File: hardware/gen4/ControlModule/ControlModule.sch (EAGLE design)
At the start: 39 parts, among them IC1 XMEGA16A4A

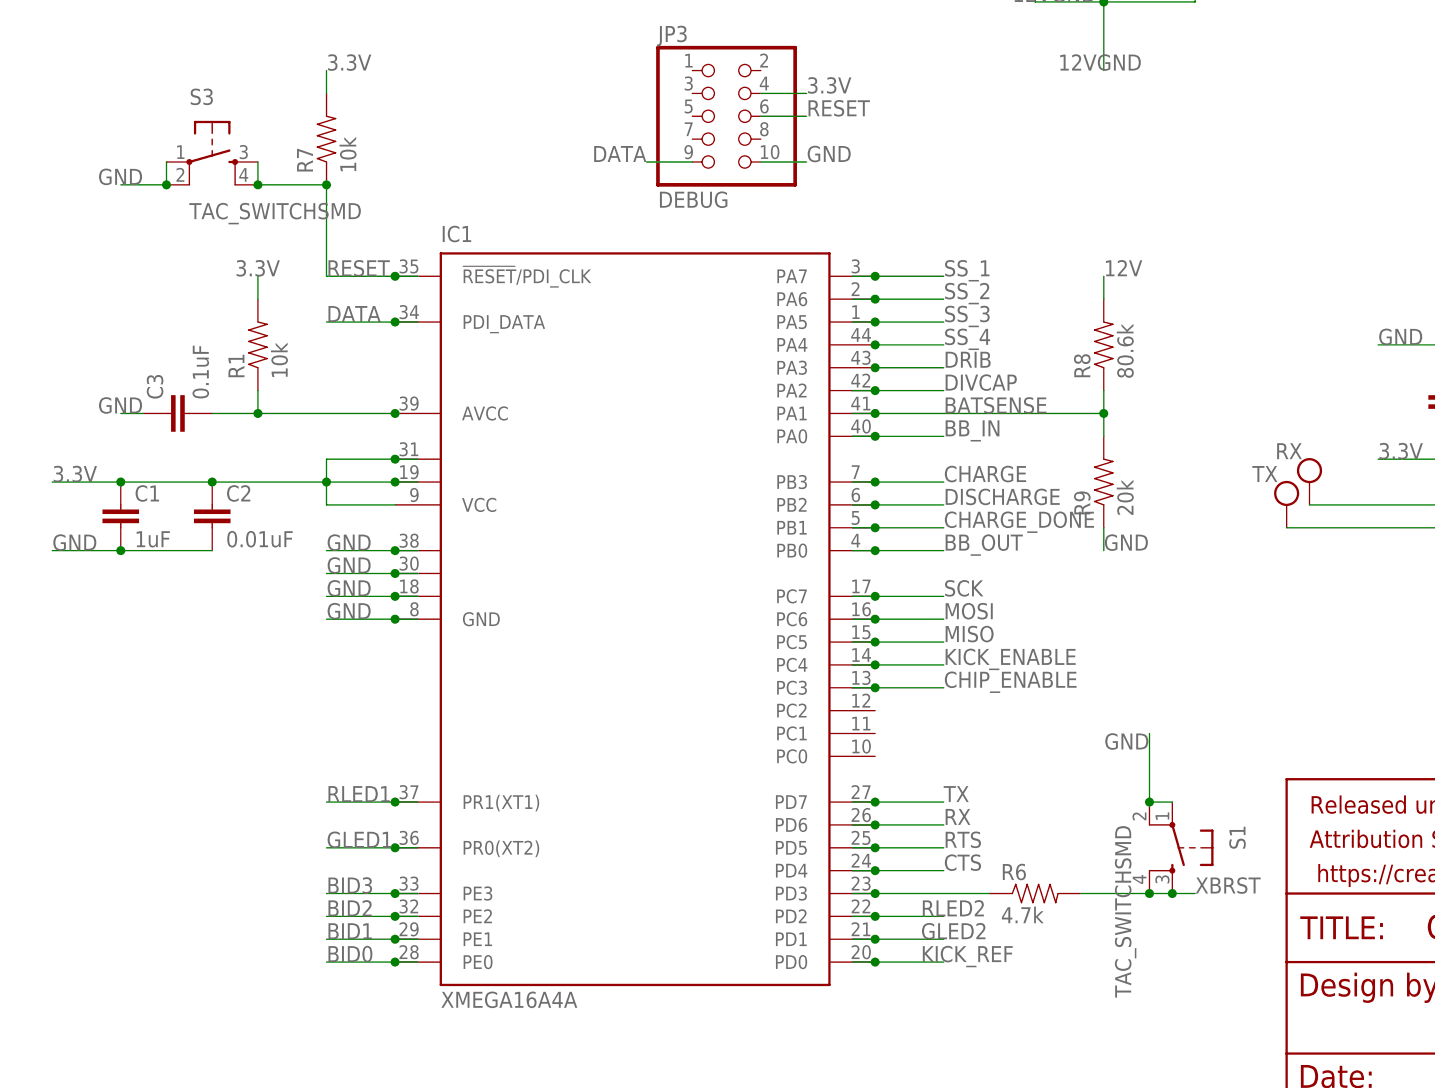
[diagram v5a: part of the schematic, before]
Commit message: fixed pushbutton on comms board
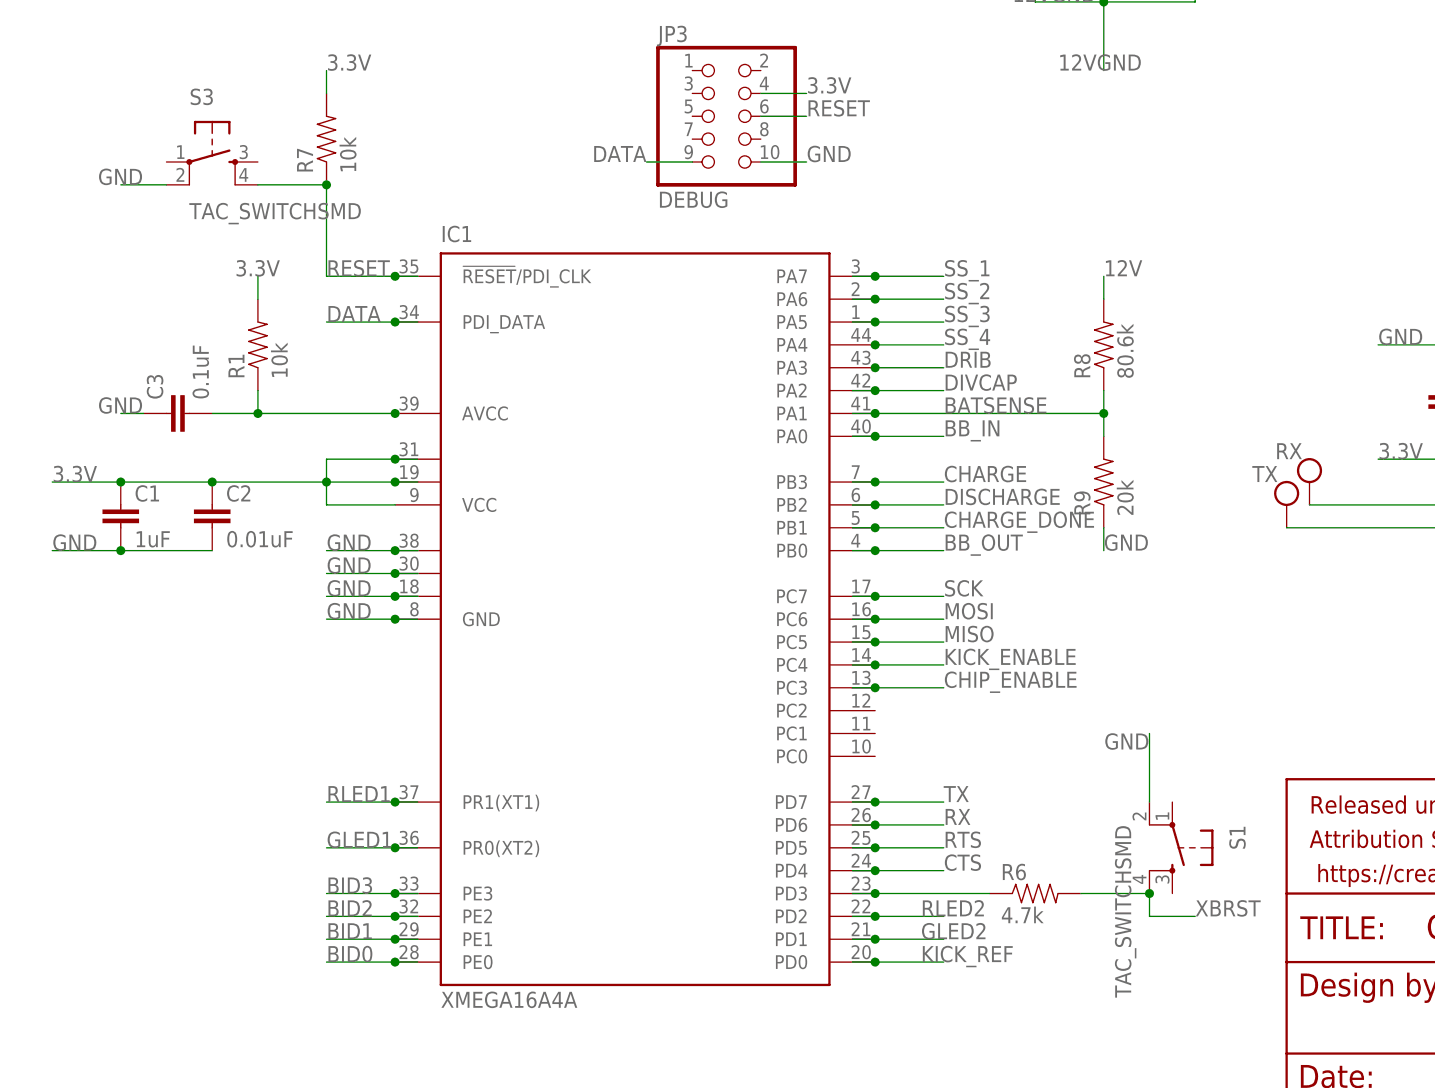
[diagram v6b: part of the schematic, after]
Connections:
- net GND: no longer S1.1, S3.1
- net RESET: no longer S3.3
- net XBRST: no longer S1.3
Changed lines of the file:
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@@
 <?xml version="1.0" encoding="utf-8"?>
 <!DOCTYPE eagle SYSTEM "eagle.dtd">
-<eagle version="7.5.0">
+<eagle version="7.2.0">
 <drawing>
 <settings>
@@
 <pinref part="R7" gate="G$1" pin="1"/>
 <pinref part="S3" gate="S" pin="4"/>
-<pinref part="S3" gate="S" pin="3"/>
-<wire x1="33.02" y1="104.14" x2="33.02" y2="101.6" width="0.1524" layer="91"/>
-<junction x="33.02" y="101.6"/>
 </segment>
 <segment>
@@
 <label x="132.08" y="40.64" size="1.778" layer="95" rot="R180"/>
 <pinref part="S1" gate="S" pin="2"/>
-<pinref part="S1" gate="S" pin="1"/>
-<wire x1="132.08" y1="33.02" x2="134.62" y2="33.02" width="0.1524" layer="91"/>
-<junction x="132.08" y="33.02"/>
 </segment>
 <segment>
@@
 <label x="15.24" y="101.6" size="1.778" layer="95"/>
 <pinref part="S3" gate="S" pin="2"/>
-<pinref part="S3" gate="S" pin="1"/>
-<wire x1="22.86" y1="104.14" x2="22.86" y2="101.6" width="0.1524" layer="91"/>
-<junction x="22.86" y="101.6"/>
 </segment>
 <segment>
@@
 <pinref part="R6" gate="G$1" pin="2"/>
 <wire x1="124.46" y1="22.86" x2="132.08" y2="22.86" width="0.1524" layer="91"/>
-<wire x1="132.08" y1="22.86" x2="134.62" y2="22.86" width="0.1524" layer="91"/>
-<label x="137.16" y="22.86" size="1.778" layer="95"/>
-<pinref part="S1" gate="S" pin="3"/>
-<wire x1="134.62" y1="22.86" x2="137.16" y2="22.86" width="0.1524" layer="91"/>
-<junction x="134.62" y="22.86"/>
+<label x="137.16" y="20.32" size="1.778" layer="95"/>
 <pinref part="S1" gate="S" pin="4"/>
 <junction x="132.08" y="22.86"/>
-</segment>
-</net>
+<wire x1="137.16" y1="20.32" x2="132.08" y2="20.32" width="0.1524" layer="91"/>
+<wire x1="132.08" y1="20.32" x2="132.08" y2="22.86" width="0.1524" layer="91"/>
+</segment>
+</net>

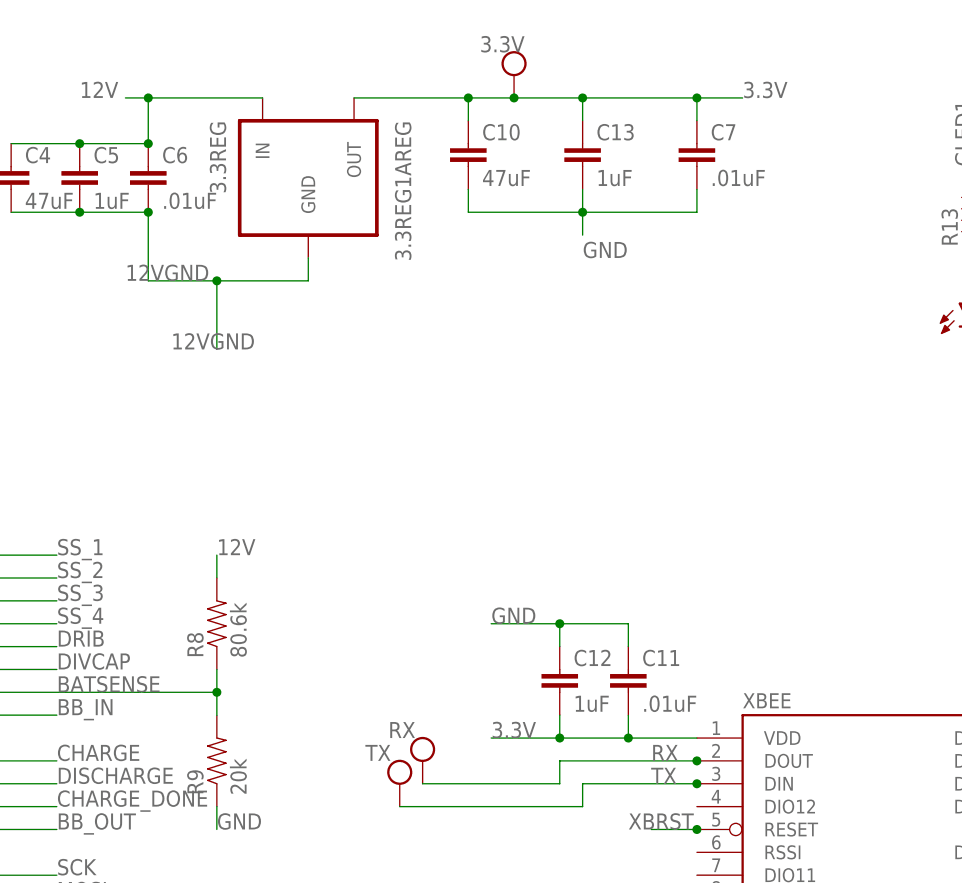
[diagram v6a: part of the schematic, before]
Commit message: fixed minor detail about capacitor sizes (using 0.01uF everywhere instead of .01uF on comms)
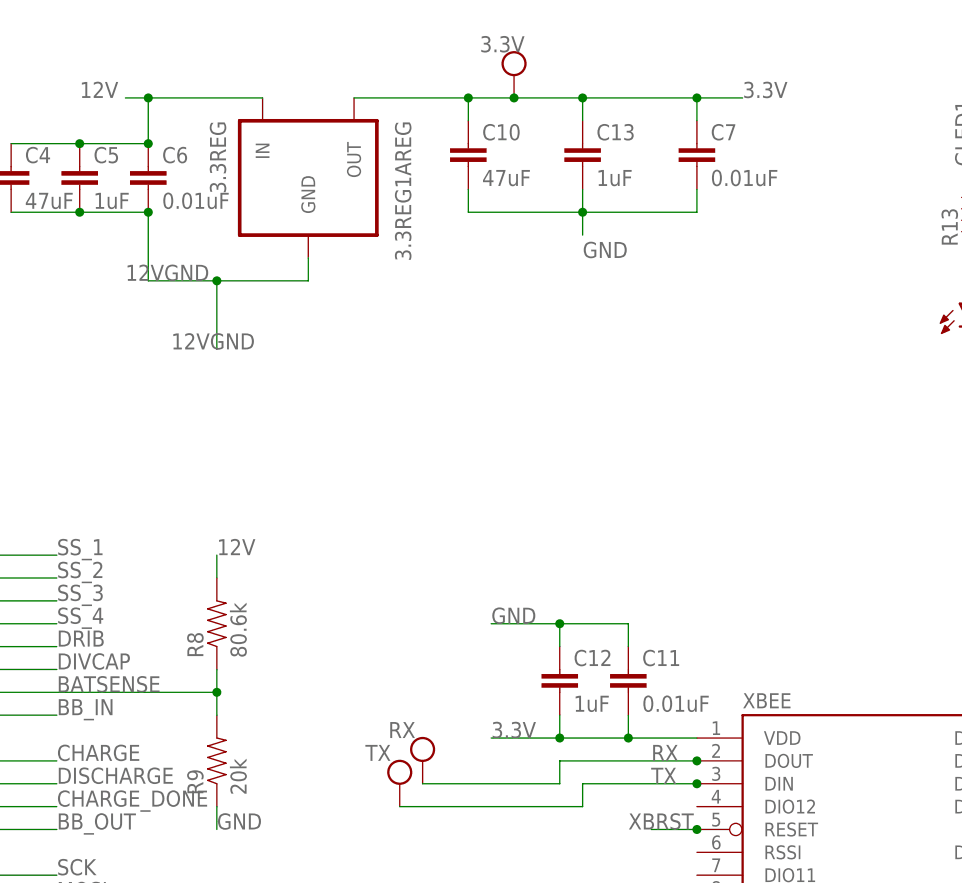
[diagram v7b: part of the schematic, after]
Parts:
- C11, C6, C7: value .01uF -> 0.01uF
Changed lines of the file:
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@@
 <part name="U$1" library="SparkFun-Electromechanical" deviceset="4-POS-DIP" device=""/>
 <part name="XBEE" library="SparkFun-RF" deviceset="XBEE-1" device="B1"/>
-<part name="C11" library="SparkFun-Capacitors" deviceset="CAP" device="0805" value=".01uF"/>
+<part name="C11" library="SparkFun-Capacitors" deviceset="CAP" device="0805" value="0.01uF"/>
 <part name="C12" library="SparkFun-Capacitors" deviceset="CAP" device="0805" value="1uF"/>
 <part name="RX" library="gen3" deviceset="TEST_PT" device=""/>
@@
 <part name="3.3V" library="gen3" deviceset="TEST_PT" device=""/>
 <part name="3.3REG" library="gen3" deviceset="3.3REG1A" device="REG"/>
-<part name="C7" library="SparkFun-Capacitors" deviceset="CAP" device="0805" value=".01uF"/>
+<part name="C7" library="SparkFun-Capacitors" deviceset="CAP" device="0805" value="0.01uF"/>
 <part name="C10" library="SparkFun-Capacitors" deviceset="CAP" device="1206" value="47uF"/>
 <part name="R2" library="SparkFun-Resistors" deviceset="RESISTOR" device="0805-RES" value="4.7k"/>
@@
 <part name="C4" library="SparkFun-Capacitors" deviceset="CAP" device="1206" value="47uF"/>
 <part name="C5" library="SparkFun-Capacitors" deviceset="CAP" device="0805" value="1uF"/>
-<part name="C6" library="SparkFun-Capacitors" deviceset="CAP" device="0805" value=".01uF"/>
+<part name="C6" library="SparkFun-Capacitors" deviceset="CAP" device="0805" value="0.01uF"/>
 <part name="JP1" library="SparkFun-Connectors" deviceset="M20X2" device="SHROUDED_SMT"/>
 <part name="S3" library="SparkFun-Retired" deviceset="TAC_SWITCH" device="SMD" value="TAC_SWITCHSMD"/>

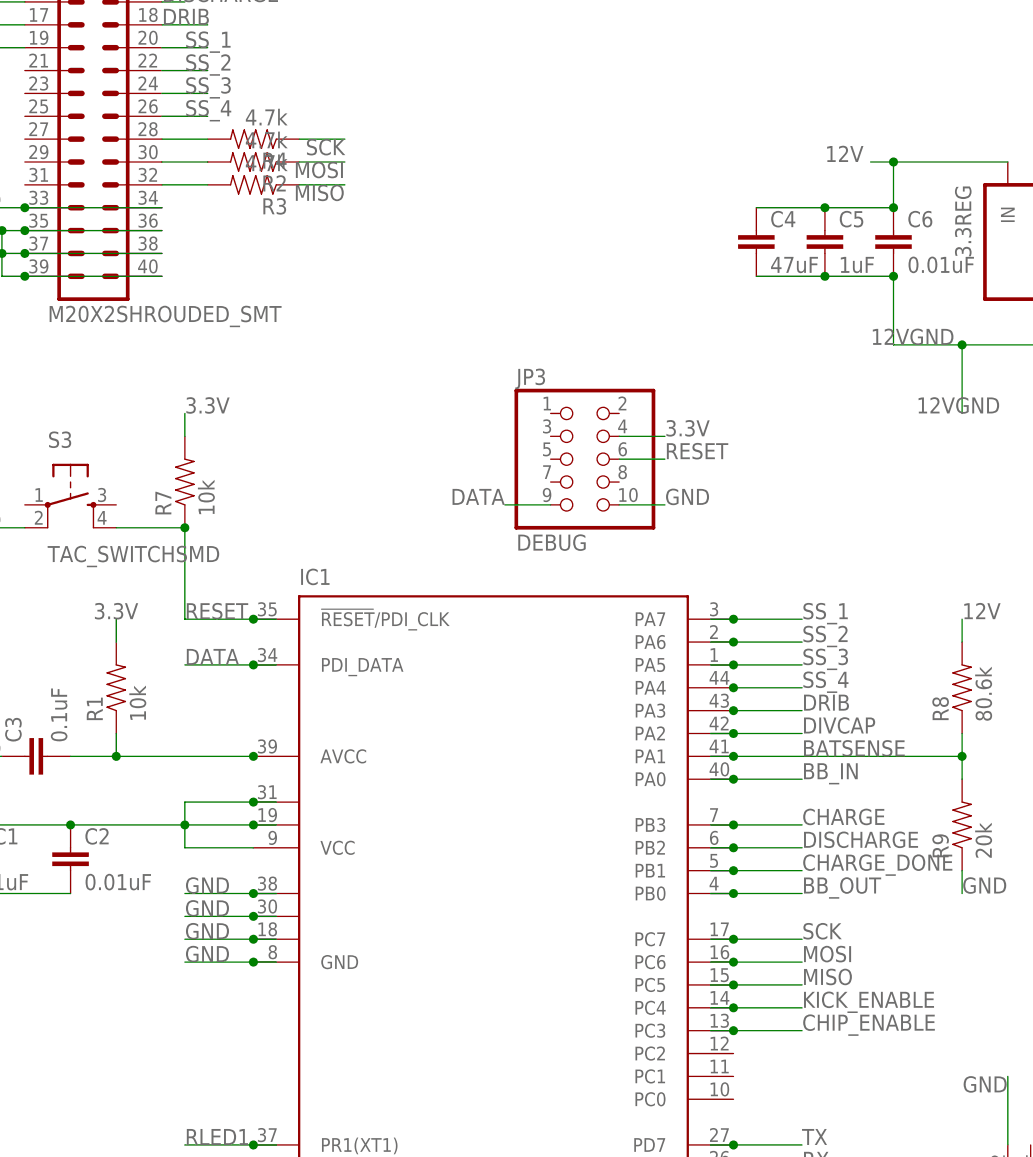
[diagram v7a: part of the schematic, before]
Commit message: fixed SPI connnections
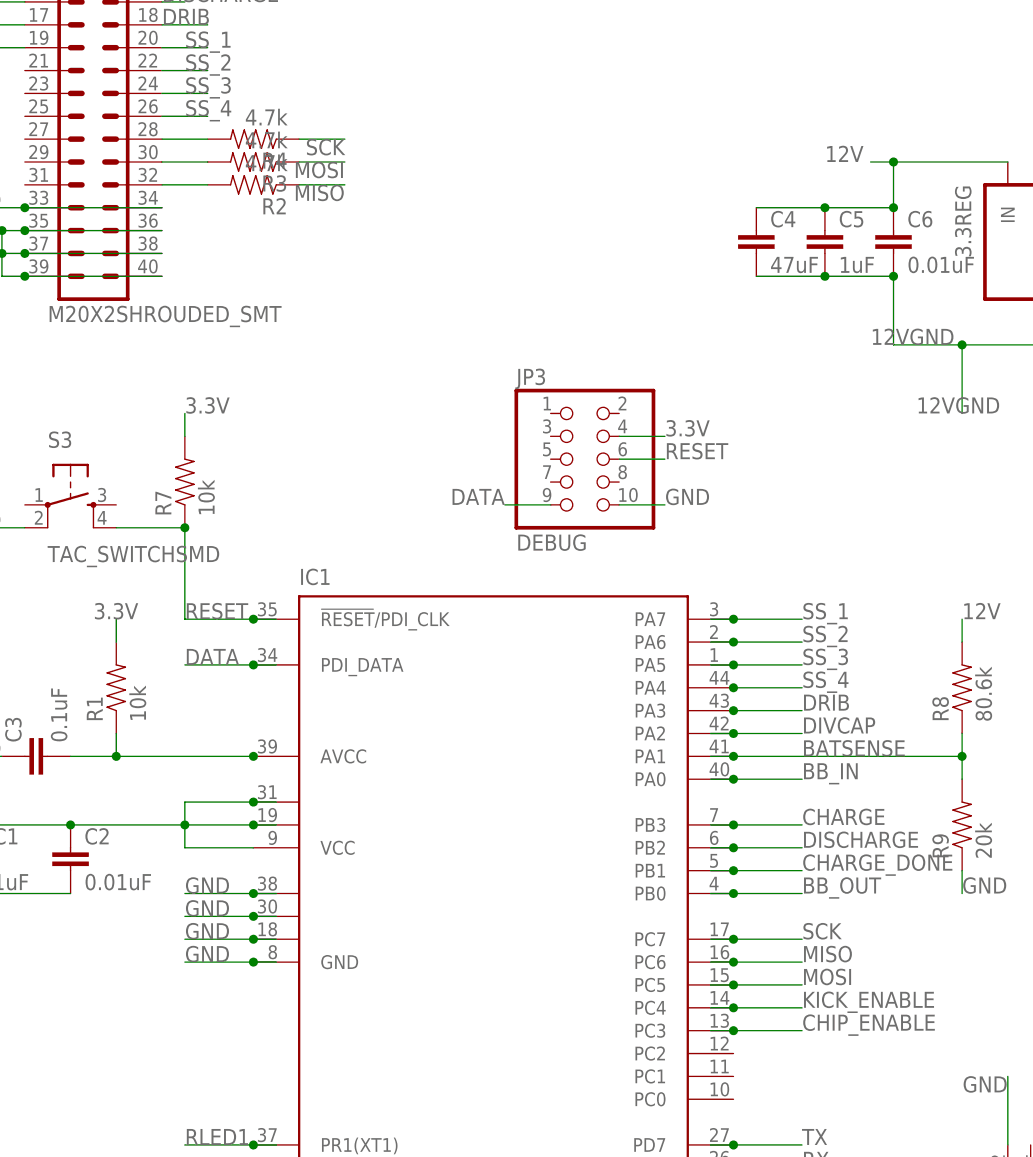
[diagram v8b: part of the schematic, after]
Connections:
- removed net N$6: JP1.30, R2.2
- removed net N$7: JP1.32, R3.2
- new net N$1: JP1.32, R2.2
- new net N$3: JP1.30, R3.2
- net MISO: now also IC1.PC6, R2.1; no longer IC1.PC5, R3.1
- net MOSI: now also IC1.PC5, R3.1; no longer IC1.PC6, R2.1
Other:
- moved on the sheet: R2, R3
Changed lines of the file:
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@@
 <instance part="C7" gate="G$1" x="180.34" y="134.62"/>
 <instance part="C10" gate="G$1" x="154.94" y="134.62"/>
-<instance part="R2" gate="G$1" x="48.26" y="142.24" rot="R180"/>
-<instance part="R3" gate="G$1" x="48.26" y="139.7" rot="R180"/>
+<instance part="R2" gate="G$1" x="48.26" y="139.7" rot="R180"/>
+<instance part="R3" gate="G$1" x="48.26" y="142.24" rot="R180"/>
 <instance part="R4" gate="G$1" x="48.26" y="144.78" rot="R180"/>
 <instance part="R13" gate="G$1" x="210.82" y="129.54" rot="R90"/>
@@
 </busses>
 <nets>
-<net name="MISO" class="0">
+<net name="MOSI" class="0">
 <segment>
 <wire x1="99.06" y1="50.8" x2="101.6" y2="50.8" width="0.1524" layer="91"/>
@@
 <segment>
 <pinref part="R3" gate="G$1" pin="1"/>
-<wire x1="53.34" y1="139.7" x2="58.42" y2="139.7" width="0.1524" layer="91"/>
-<label x="58.42" y="139.7" size="1.778" layer="95" rot="R180"/>
-</segment>
-</net>
-<net name="MOSI" class="0">
+<wire x1="53.34" y1="142.24" x2="58.42" y2="142.24" width="0.1524" layer="91"/>
+<label x="58.42" y="142.24" size="1.778" layer="95" rot="R180"/>
+</segment>
+</net>
+<net name="MISO" class="0">
 <segment>
 <wire x1="99.06" y1="53.34" x2="101.6" y2="53.34" width="0.1524" layer="91"/>
@@
 <segment>
 <pinref part="R2" gate="G$1" pin="1"/>
-<wire x1="53.34" y1="142.24" x2="58.42" y2="142.24" width="0.1524" layer="91"/>
-<label x="58.42" y="142.24" size="1.778" layer="95" rot="R180"/>
+<wire x1="53.34" y1="139.7" x2="58.42" y2="139.7" width="0.1524" layer="91"/>
+<label x="58.42" y="139.7" size="1.778" layer="95" rot="R180"/>
 </segment>
 </net>
@@
 </segment>
 </net>
-<net name="N$6" class="0">
-<segment>
-<pinref part="R2" gate="G$1" pin="2"/>
-<wire x1="38.1" y1="142.24" x2="43.18" y2="142.24" width="0.1524" layer="91"/>
-<pinref part="JP1" gate="G$1" pin="30"/>
-</segment>
-</net>
-<net name="N$7" class="0">
-<segment>
-<pinref part="R3" gate="G$1" pin="2"/>
-<wire x1="38.1" y1="139.7" x2="43.18" y2="139.7" width="0.1524" layer="91"/>
-<pinref part="JP1" gate="G$1" pin="32"/>
-</segment>
-</net>
 <net name="N$8" class="0">
 <segment>
@@
 </segment>
 </net>
+<net name="N$1" class="0">
+<segment>
+<pinref part="JP1" gate="G$1" pin="32"/>
+<pinref part="R2" gate="G$1" pin="2"/>
+<wire x1="38.1" y1="139.7" x2="43.18" y2="139.7" width="0.1524" layer="91"/>
+</segment>
+</net>
+<net name="N$3" class="0">
+<segment>
+<pinref part="R3" gate="G$1" pin="2"/>
+<pinref part="JP1" gate="G$1" pin="30"/>
+<wire x1="43.18" y1="142.24" x2="38.1" y2="142.24" width="0.1524" layer="91"/>
+</segment>
+</net>
